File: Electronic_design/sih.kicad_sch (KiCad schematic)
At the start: 20 parts, among them U1 ESP32-D0WD, U2 AP2112K-3.3, U3 TP4057, U4 LM358, Y1 40MHz

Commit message: PCB design and schematic modified
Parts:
- BT1: footprint Battery:BatteryHolder_Keystone_103_1x20mm -> Battery:BatteryHolder_Keystone_2998_1x6.8mm
- RV1: value R_Potentiometer -> 10 K
- U3: footprint Package_SO:SOIC-8-1EP_3.9x4.9mm_P1.27mm_EP2.29x3mm -> Package_TO_SOT_SMD:SOT-23-6
- U4: footprint Package_DIP:DIP-8-16_W7.62mm -> Package_SO:SOIC-8-1EP_3.9x4.9mm_P1.27mm_EP2.29x3mm
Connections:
- net 3.3V is gone; now on an unnamed net: R2.2, R3.1
- net GND: no longer C7.2, R3.2, R4.2, RV1.2, U4.3 (+)
- new net: C7.2, R3.2, R4.2, RV1.2, U4.3 (+)
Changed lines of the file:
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@@
 	(paper "A4")
-	(junction
-		(at 257.81 43.18)
-		(diameter 0)
-		(color 0 0 0 0)
-	)
 	(junction
 		(at 265.43 69.85)
@@
 	)
 	(junction
-		(at 257.81 35.56)
-		(diameter 0)
-		(color 0 0 0 0)
-	)
-	(junction
 		(at 109.22 137.16)
 		(diameter 0)
@@
 	)
 	(junction
+		(at 127 45.72)
+		(diameter 0)
+		(color 0 0 0 0)
+	)
+	(junction
 		(at 107.95 48.26)
 		(diameter 0)
@@
 		(color 0 0 0 0)
 	)
-	(junction
-		(at 107.95 139.7)
-		(diameter 0)
-		(color 0 0 0 0)
-	)
 	(wire
 		(pts
@@
 	(wire
 		(pts
-			(xy 257.81 43.18) (xy 257.81 35.56)
+			(xy 127 45.72) (xy 127 48.26)
 		)
 		(stroke
@@
 	(wire
 		(pts
+			(xy 193.04 69.85) (xy 182.88 69.85)
+		)
+		(stroke
+			(width 0)
+			(type default)
+		)
+	)
+	(wire
+		(pts
 			(xy 20.32 57.15) (xy 29.21 57.15)
 		)
@@
 	(wire
 		(pts
-			(xy 193.04 68.58) (xy 193.04 69.85)
-		)
-		(stroke
-			(width 0)
-			(type default)
-		)
-	)
-	(wire
-		(pts
 			(xy 252.73 46.99) (xy 247.65 46.99)
 		)
@@
 	(wire
 		(pts
+			(xy 182.88 45.72) (xy 127 45.72)
+		)
+		(stroke
+			(width 0)
+			(type default)
+		)
+	)
+	(wire
+		(pts
 			(xy 158.75 137.16) (xy 140.97 137.16)
 		)
@@
 	(wire
 		(pts
-			(xy 127 38.1) (xy 127 48.26)
+			(xy 127 38.1) (xy 127 45.72)
 		)
 		(stroke
@@
 	(wire
 		(pts
-			(xy 107.95 138.43) (xy 107.95 139.7)
-		)
-		(stroke
-			(width 0)
-			(type default)
-		)
-	)
-	(wire
-		(pts
 			(xy 158.75 67.31) (xy 158.75 90.17)
 		)
@@
 		(pts
 			(xy 105.41 48.26) (xy 107.95 48.26)
+		)
+		(stroke
+			(width 0)
+			(type default)
+		)
+	)
+	(wire
+		(pts
+			(xy 182.88 69.85) (xy 182.88 45.72)
 		)
 		(stroke
@@
 	(symbol
 		(lib_id "power:VCC")
-		(at 193.04 68.58 0)
-		(unit 1)
-		(exclude_from_sim no)
-		(in_bom yes)
-		(on_board yes)
-		(dnp no)
-		(fields_autoplaced yes)
-		(property "Reference" "#PWR04"
-			(at 193.04 72.39 0)
-			(effects
-				(font
-					(size 1.27 1.27)
-				)
-				(hide yes)
-			)
-		)
-		(property "Value" "3.3V"
-			(at 193.04 63.5 0)
-			(effects
-				(font
-					(size 1.27 1.27)
-				)
-			)
-		)
-		(property "Footprint" ""
-			(at 193.04 68.58 0)
-			(effects
-				(font
-					(size 1.27 1.27)
-				)
-				(hide yes)
-			)
-		)
-		(property "Datasheet" ""
-			(at 193.04 68.58 0)
-			(effects
-				(font
-					(size 1.27 1.27)
-				)
-				(hide yes)
-			)
-		)
-		(property "Description" "Power symbol creates a global label with name \"VCC\""
-			(at 193.04 68.58 0)
-			(effects
-				(font
-					(size 1.27 1.27)
-				)
-				(hide yes)
-			)
-		)
-		(pin "1"
-		)
-		(instances
-			(project "sih"
-				(path "/30865b9b-37c5-4f37-aecd-20f80092d846"
-					(reference "#PWR04")
-					(unit 1)
-				)
-			)
-		)
-	)
-	(symbol
-		(lib_id "power:VCC")
 		(at 107.95 46.99 0)
 		(unit 1)
@@
 			)
 		)
-		(property "Value" "R_Potentiometer"
+		(property "Value" "10 K"
 			(at 228.6 41.91 90)
 			(effects
@@
 			)
 		)
-		(property "Footprint" "Package_SO:SOIC-8-1EP_3.9x4.9mm_P1.27mm_EP2.29x3mm"
+		(property "Footprint" "Package_TO_SOT_SMD:SOT-23-6"
 			(at 140.97 76.2 0)
 			(effects
@@
 			)
 		)
-		(property "Footprint" "Package_DIP:DIP-8-16_W7.62mm"
+		(property "Footprint" "Package_SO:SOIC-8-1EP_3.9x4.9mm_P1.27mm_EP2.29x3mm"
 			(at 255.27 69.85 0)
 			(effects
@@
 			)
 		)
-		(property "Footprint" "Battery:BatteryHolder_Keystone_103_1x20mm"
+		(property "Footprint" "Battery:BatteryHolder_Keystone_2998_1x6.8mm"
 			(at 158.75 60.706 90)
 			(effects
@@
 		(on_board yes)
 		(dnp no)
-		(fields_autoplaced yes)
 		(property "Reference" "Y1"
-			(at 26.67 71.1199 90)
+			(at 16.256 75.184 90)
 			(effects
 				(font
@@
 		)
 		(property "Value" "40MHz"
-			(at 26.67 73.6599 90)
-			(effects
-				(font
+			(at 16.256 77.724 90)
+			(effects
+				(font

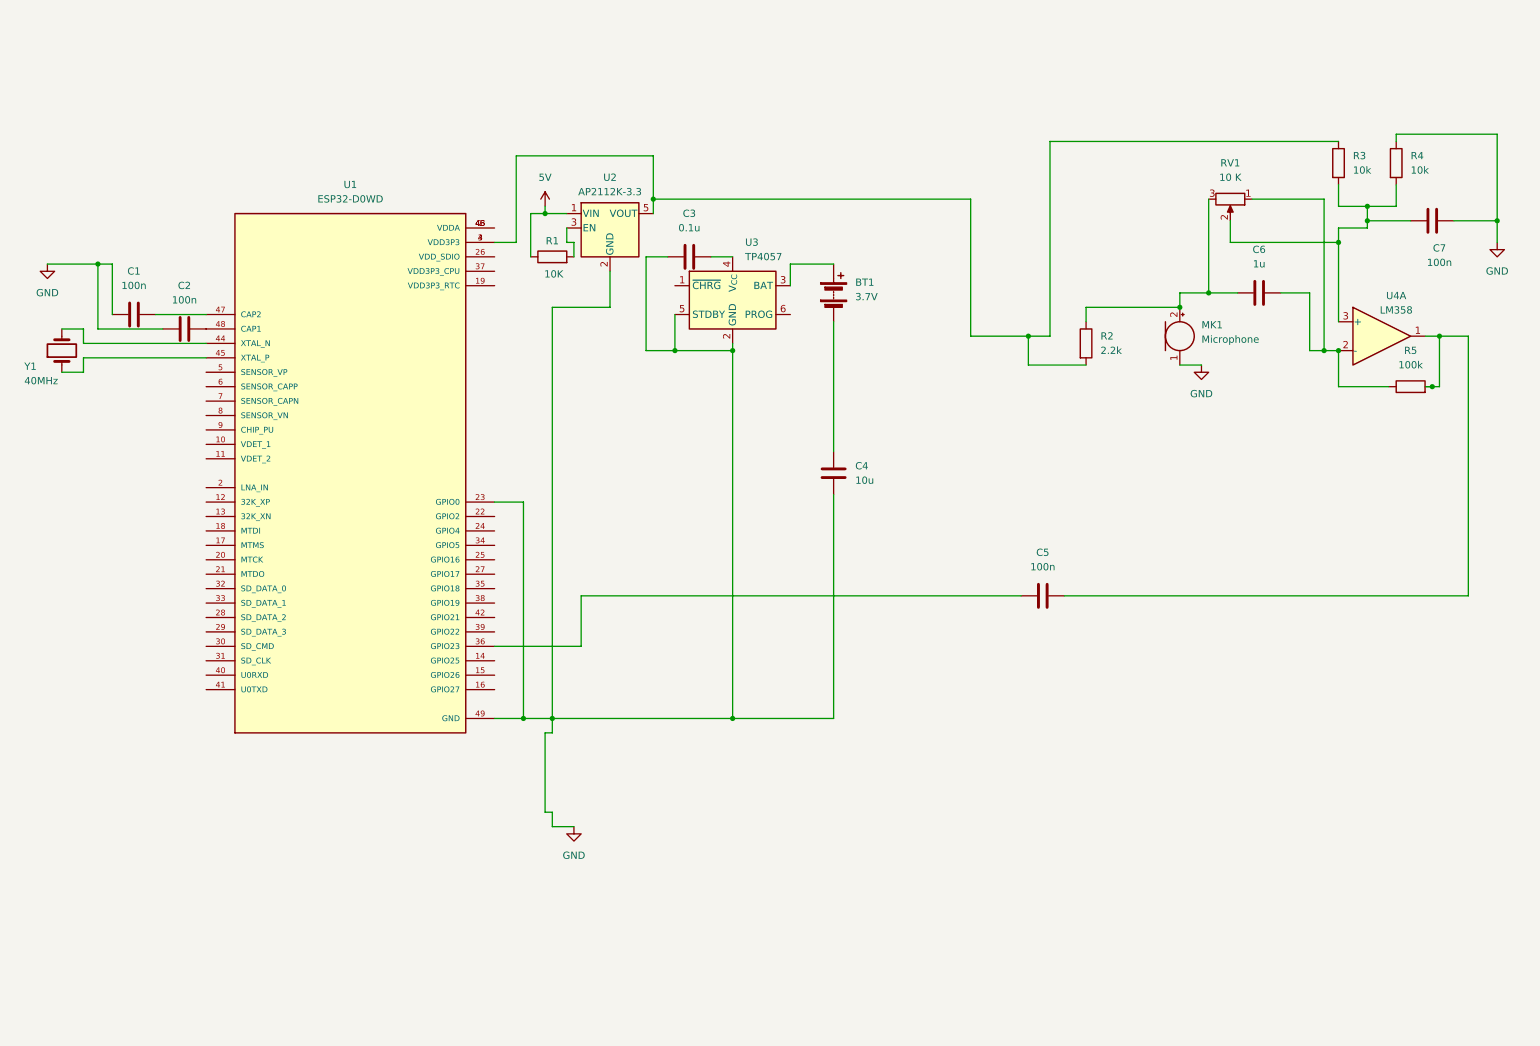
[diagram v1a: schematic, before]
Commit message: Updated design with all components
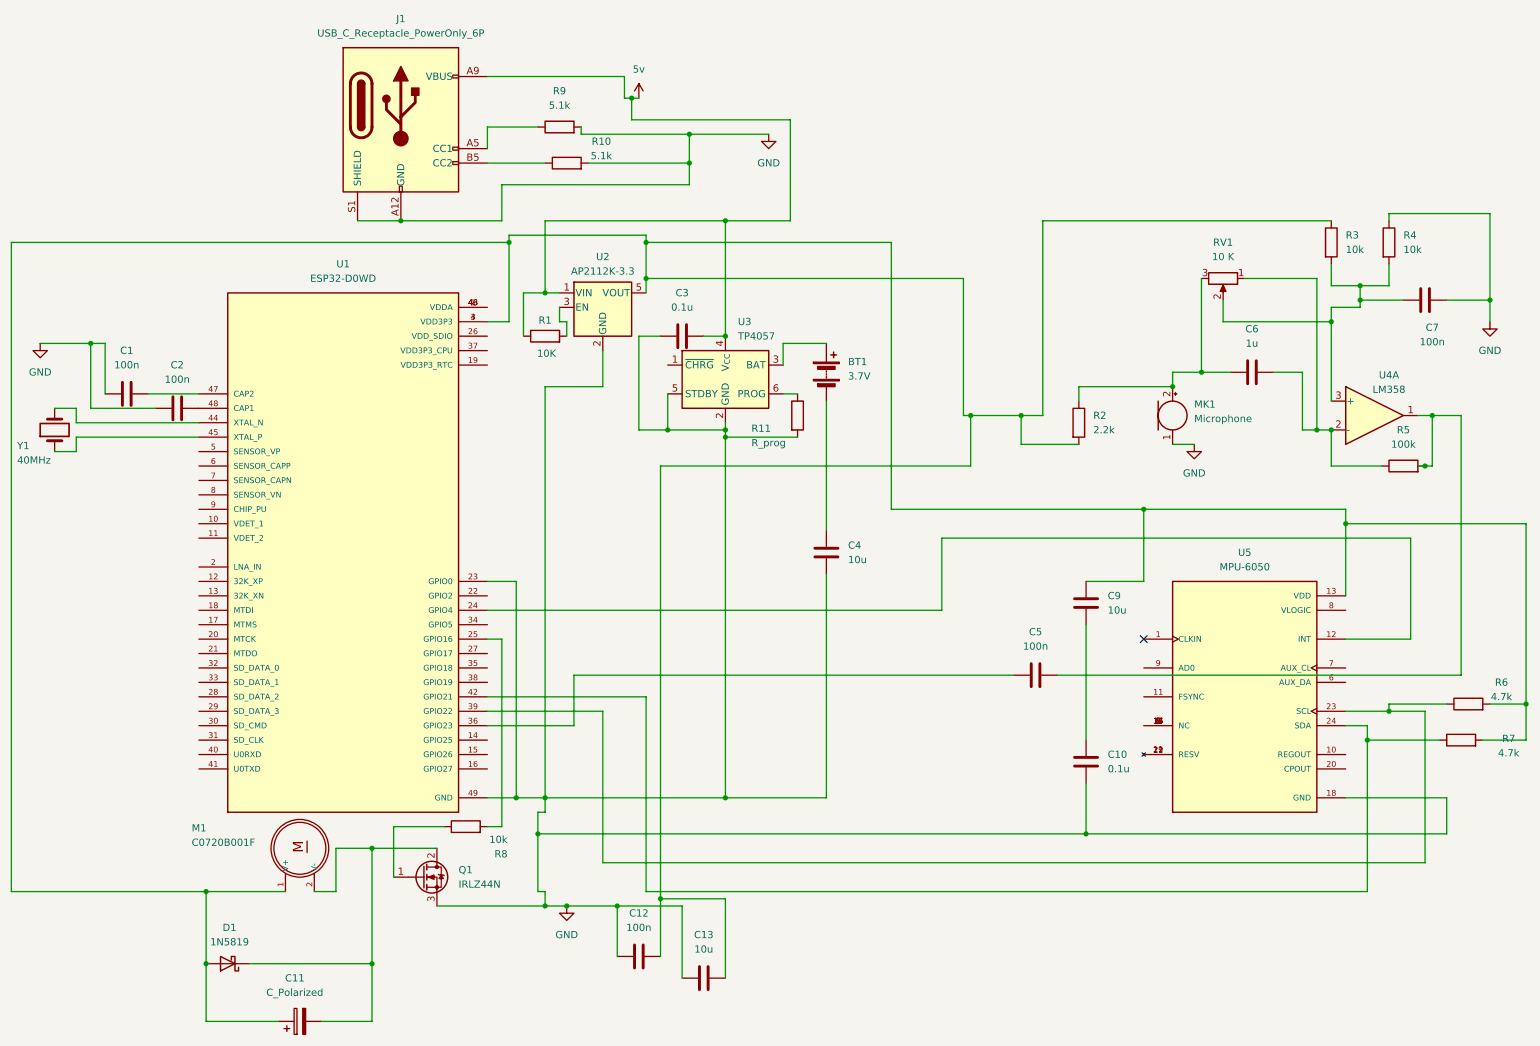
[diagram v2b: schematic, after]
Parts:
- added C10: 0.1u, Capacitor_SMD:C_0603_1608Metric, symbol Device:C
- added C11: C_Polarized, Capacitor_SMD:C_Elec_3x5.4, symbol Device:C_Polarized
- added C12: 100n, Capacitor_SMD:C_0603_1608Metric, symbol Device:C
- added C13, C9: 10u, Capacitor_SMD:C_0603_1608Metric, symbol Device:C
- added D1: 1N5819, Diode_THT:D_DO-41_SOD81_P10.16mm_Horizontal, symbol Diode:1N5819
- added J1: USB_C_Receptacle_PowerOnly_6P, Connector_USB:USB_C_Receptacle_Amphenol_12401548E4-2A, symbol Connector:USB_C_Receptacle_PowerOnly_6P
- added M1: C0720B001F, C0720B001F:XDCR_C0720B001F, symbol C0720B001F:C0720B001F
- added Q1: IRLZ44N, Package_TO_SOT_SMD:SOT-223, symbol Transistor_FET:IRLZ44N
- added R10, R9: 5.1k, Resistor_SMD:R_0603_1608Metric, symbol Device:R
- added R11: R_prog, Resistor_SMD:R_0603_1608Metric, symbol Device:R
- added R6, R7: 4.7k, Resistor_SMD:R_0603_1608Metric, symbol Device:R
- added R8: 10k, Resistor_SMD:R_0603_1608Metric, symbol Device:R
- added U5: MPU-6050, MPU-6050:QFN50P400X400X95-24N, symbol MPU-6050:MPU-6050
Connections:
- net 5V is gone; now on net 5v: R1.1, U2.1 (VIN)
- net GND: now also C10.2, C12.1, C13.1, J1.A12 (GND), J1.B12 (GND), J1.S1 (SHIELD), Q1.3 (S), R10.2, R11.2, R9.2, U5.18 (GND)
- net 5v: now reaches C3.2, U3.4 (V_{CC})
- net 5v: now also J1.A9 (VBUS), J1.B9 (VBUS)
- net at U3.6 (PROG): now also R11.1
- net at R2.2, R3.1, U1.3 (VDD3P3)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: now also C11.1, C12.2, C13.2, C9.1, D1.2 (A), M1.1 (V+), R6.2, R7.2, U5.13 (VDD)
- net at U1.24 (GPIO4): now also U5.12 (INT)
- net at U1.25 (GPIO16): now also R8.2
- net at U1.39 (GPIO22): now also R6.1, U5.23 (SCL)
- net at U1.42 (GPIO21): now also R7.1, U5.24 (SDA)
- new net: J1.B5 (CC2), R10.1
- new net: C10.1, C9.2
- new net: J1.A5 (CC1), R9.1
- new net: C11.2, D1.1 (K), M1.2 (V-), Q1.2 (D)
- new net: Q1.1 (G), R8.1
- new net: U5.14 (NC), U5.15 (NC), U5.16 (NC), U5.17 (NC), U5.2 (NC), U5.3 (NC), U5.4 (NC), U5.5 (NC)
- new net: U5.19 (RESV), U5.21 (RESV), U5.22 (RESV)
- no-connect marks 0 -> 1
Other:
- moved on the sheet: BT1, C1, C2, C3, C4, C5, C6, C7, MK1, R1, R2, R3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
